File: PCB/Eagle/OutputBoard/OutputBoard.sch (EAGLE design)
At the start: 19 parts

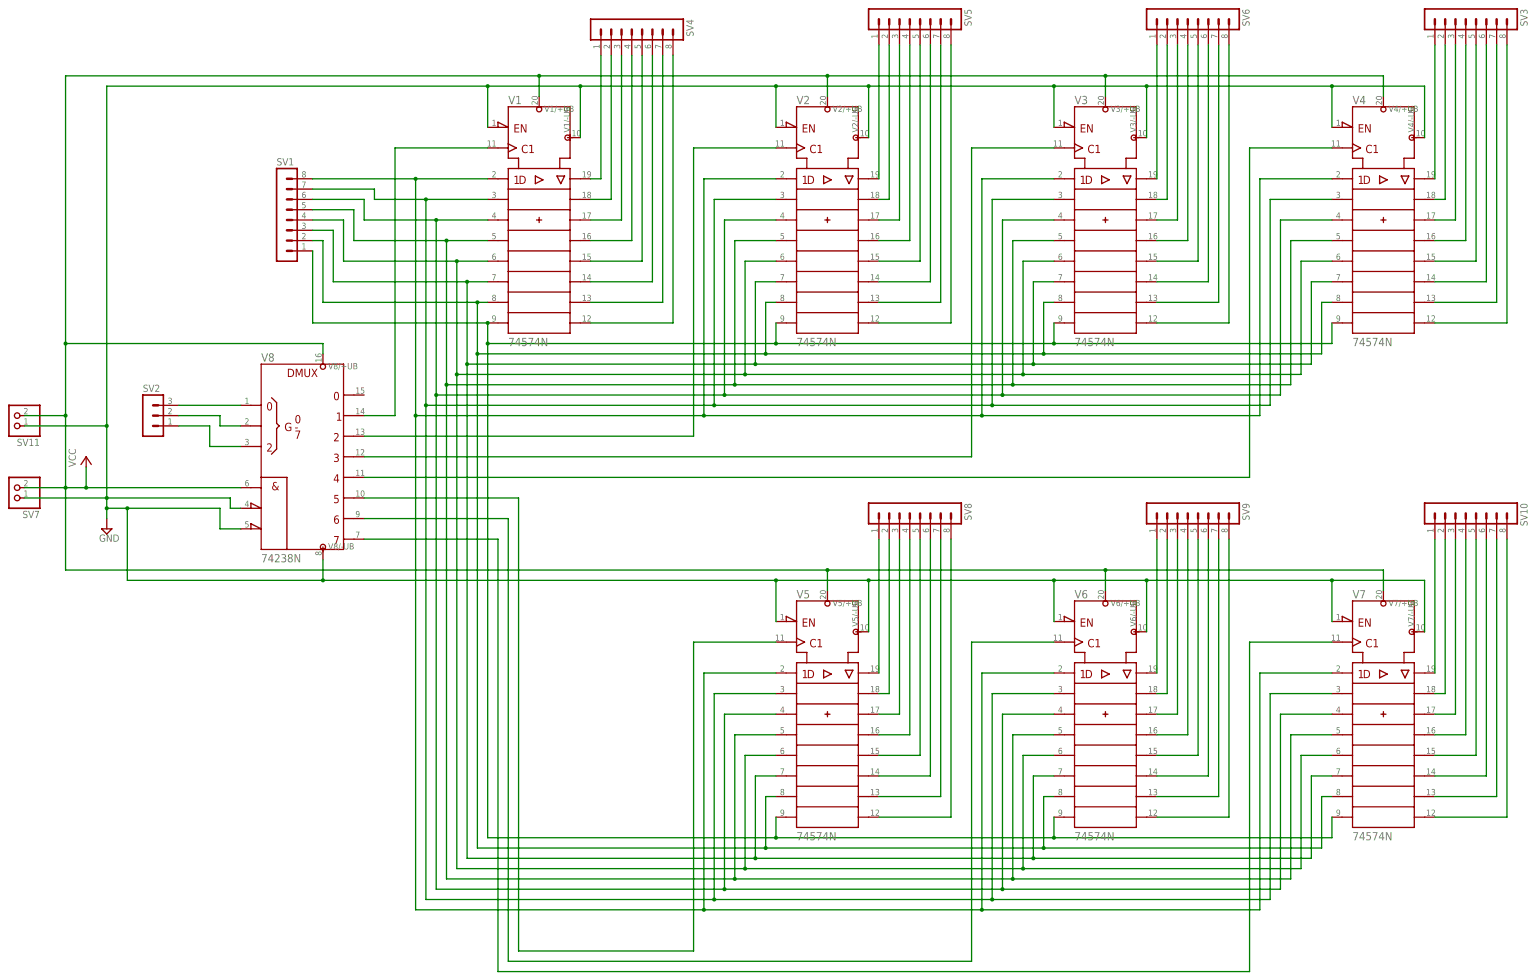
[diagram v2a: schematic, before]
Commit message: PCB Modified with proper flip flop 74 273 and ground fill
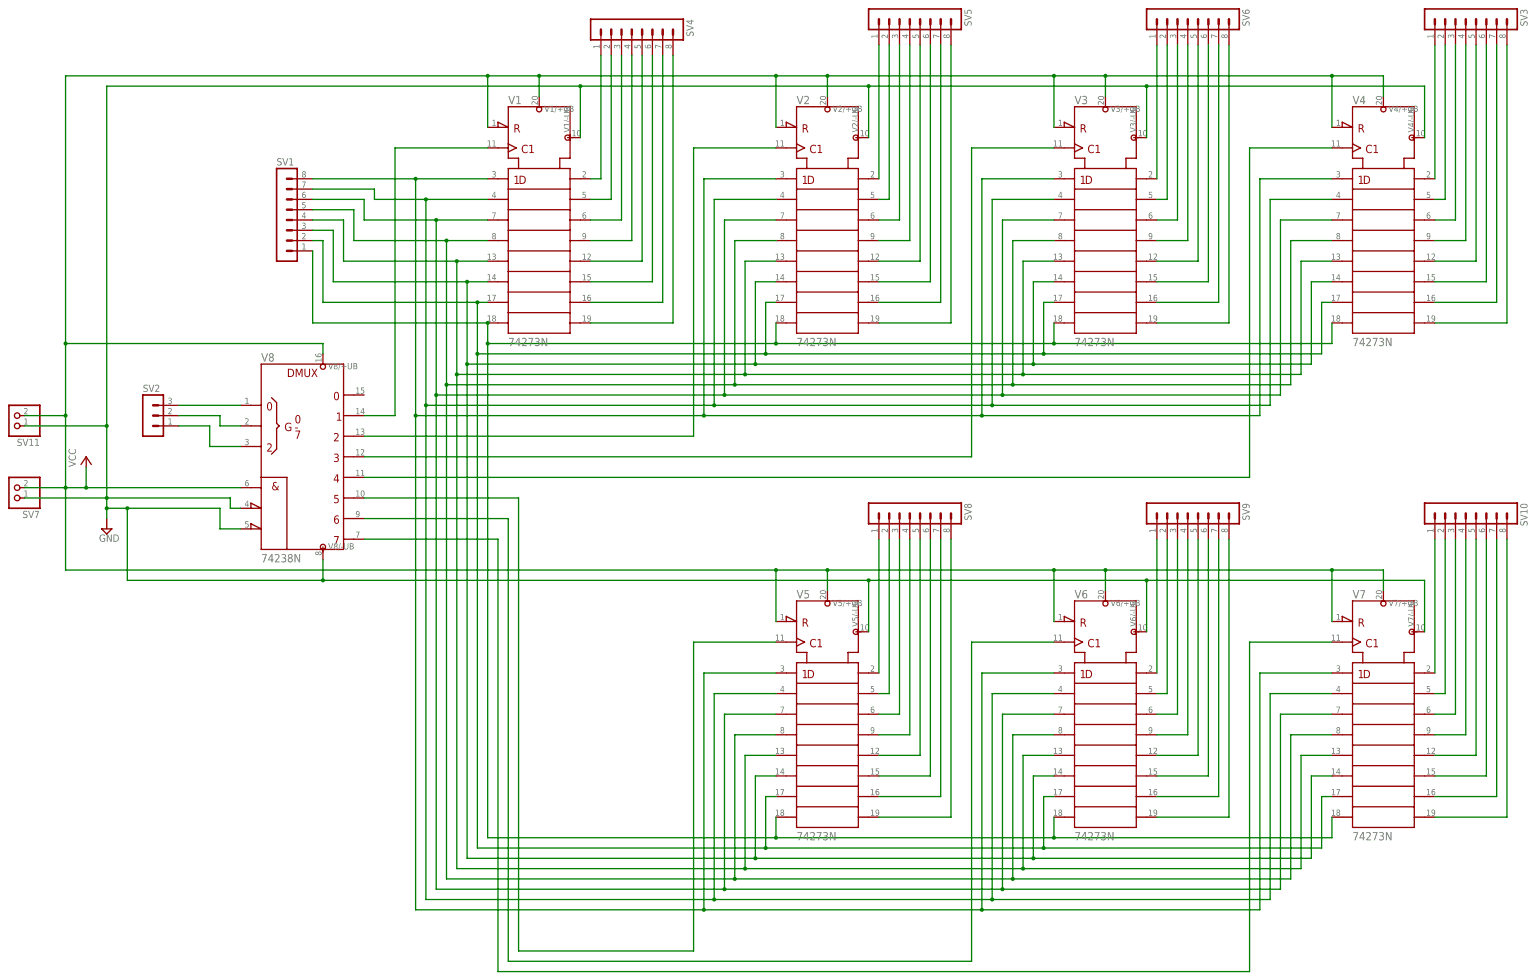
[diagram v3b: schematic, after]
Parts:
- V1, V2, V3, V4, V5, V6, V7: value 74574N -> 74273N; device 74ttl-din:74574N -> 74ttl-din:74273N
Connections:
- net GND: no longer V11.!OC, V21.!OC, V31.!OC, V41.!OC, V51.!OC, V61.!OC, V71.!OC
- net VCC: now also V11.!CLR, V21.!CLR, V31.!CLR, V41.!CLR, V51.!CLR, V61.!CLR, V71.!CLR
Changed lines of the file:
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@@
 </classes>
 <parts>
-<part name="V1" library="74ttl-din" deviceset="74*574" device="N"/>
-<part name="V2" library="74ttl-din" deviceset="74*574" device="N"/>
-<part name="V3" library="74ttl-din" deviceset="74*574" device="N"/>
+<part name="V1" library="74ttl-din" deviceset="74*273" device="N"/>
+<part name="V2" library="74ttl-din" deviceset="74*273" device="N"/>
+<part name="V3" library="74ttl-din" deviceset="74*273" device="N"/>
 <part name="SUPPLY1" library="supply2" deviceset="GND" device=""/>
 <part name="P+1" library="supply1" deviceset="VCC" device=""/>
@@
 <part name="SV6" library="con-lstb" deviceset="MA08-1" device=""/>
 <part name="SV7" library="pinhead" deviceset="PINHD-1X2" device=""/>
-<part name="V4" library="74ttl-din" deviceset="74*574" device="N"/>
+<part name="V4" library="74ttl-din" deviceset="74*273" device="N"/>
 <part name="SV3" library="con-lstb" deviceset="MA08-1" device=""/>
-<part name="V5" library="74ttl-din" deviceset="74*574" device="N"/>
-<part name="V6" library="74ttl-din" deviceset="74*574" device="N"/>
+<part name="V5" library="74ttl-din" deviceset="74*273" device="N"/>
+<part name="V6" library="74ttl-din" deviceset="74*273" device="N"/>
 <part name="SV8" library="con-lstb" deviceset="MA08-1" device=""/>
 <part name="SV9" library="con-lstb" deviceset="MA08-1" device=""/>
-<part name="V7" library="74ttl-din" deviceset="74*574" device="N"/>
+<part name="V7" library="74ttl-din" deviceset="74*273" device="N"/>
 <part name="SV10" library="con-lstb" deviceset="MA08-1" device=""/>
 <part name="V8" library="74ttl-din" deviceset="74*238" device="N"/>
@@
 <net name="GND" class="0">
 <segment>
-<pinref part="V1" gate="1" pin="!OC"/>
-<wire x1="35.56" y1="68.58" x2="35.56" y2="78.74" width="0.1524" layer="91"/>
-<wire x1="-58.42" y1="78.74" x2="35.56" y2="78.74" width="0.1524" layer="91"/>
-<junction x="35.56" y="78.74"/>
+<wire x1="-58.42" y1="78.74" x2="58.42" y2="78.74" width="0.1524" layer="91"/>
 <pinref part="SUPPLY1" gate="GND" pin="GND"/>
 <wire x1="-58.42" y1="-27.94" x2="-58.42" y2="-25.4" width="0.1524" layer="91"/>
@@
 <pinref part="SV7" gate="G$1" pin="1"/>
 <wire x1="-78.74" y1="-22.86" x2="-58.42" y2="-22.86" width="0.1524" layer="91"/>
-<pinref part="V5" gate="1" pin="!OC"/>
-<wire x1="106.68" y1="-43.18" x2="106.68" y2="-53.34" width="0.1524" layer="91"/>
-<wire x1="106.68" y1="-43.18" x2="129.54" y2="-43.18" width="0.1524" layer="91"/>
-<pinref part="V6" gate="1" pin="!OC"/>
-<wire x1="129.54" y1="-43.18" x2="175.26" y2="-43.18" width="0.1524" layer="91"/>
-<wire x1="175.26" y1="-43.18" x2="175.26" y2="-53.34" width="0.1524" layer="91"/>
-<junction x="106.68" y="-43.18"/>
-<wire x1="175.26" y1="-43.18" x2="198.12" y2="-43.18" width="0.1524" layer="91"/>
-<pinref part="V7" gate="1" pin="!OC"/>
-<wire x1="198.12" y1="-43.18" x2="243.84" y2="-43.18" width="0.1524" layer="91"/>
-<wire x1="243.84" y1="-43.18" x2="243.84" y2="-53.34" width="0.1524" layer="91"/>
-<junction x="175.26" y="-43.18"/>
-<wire x1="106.68" y1="-43.18" x2="-5.08" y2="-43.18" width="0.1524" layer="91"/>
+<wire x1="129.54" y1="-43.18" x2="198.12" y2="-43.18" width="0.1524" layer="91"/>
+<wire x1="198.12" y1="-43.18" x2="266.7" y2="-43.18" width="0.1524" layer="91"/>
+<wire x1="129.54" y1="-43.18" x2="-5.08" y2="-43.18" width="0.1524" layer="91"/>
 <wire x1="-5.08" y1="-43.18" x2="-53.34" y2="-43.18" width="0.1524" layer="91"/>
 <wire x1="-53.34" y1="-43.18" x2="-53.34" y2="-25.4" width="0.1524" layer="91"/>
-<pinref part="V4" gate="1" pin="!OC"/>
-<wire x1="243.84" y1="78.74" x2="243.84" y2="68.58" width="0.1524" layer="91"/>
-<pinref part="V3" gate="1" pin="!OC"/>
-<pinref part="V2" gate="1" pin="!OC"/>
-<wire x1="35.56" y1="78.74" x2="58.42" y2="78.74" width="0.1524" layer="91"/>
-<wire x1="58.42" y1="78.74" x2="106.68" y2="78.74" width="0.1524" layer="91"/>
-<wire x1="106.68" y1="78.74" x2="106.68" y2="68.58" width="0.1524" layer="91"/>
-<junction x="106.68" y="78.74"/>
-<wire x1="106.68" y1="78.74" x2="129.54" y2="78.74" width="0.1524" layer="91"/>
-<wire x1="129.54" y1="78.74" x2="175.26" y2="78.74" width="0.1524" layer="91"/>
-<wire x1="175.26" y1="78.74" x2="175.26" y2="68.58" width="0.1524" layer="91"/>
-<wire x1="175.26" y1="78.74" x2="198.12" y2="78.74" width="0.1524" layer="91"/>
-<junction x="175.26" y="78.74"/>
-<wire x1="198.12" y1="78.74" x2="243.84" y2="78.74" width="0.1524" layer="91"/>
+<wire x1="58.42" y1="78.74" x2="129.54" y2="78.74" width="0.1524" layer="91"/>
+<wire x1="129.54" y1="78.74" x2="198.12" y2="78.74" width="0.1524" layer="91"/>
+<wire x1="198.12" y1="78.74" x2="266.7" y2="78.74" width="0.1524" layer="91"/>
 <wire x1="-58.42" y1="-22.86" x2="-27.94" y2="-22.86" width="0.1524" layer="91"/>
 <wire x1="-27.94" y1="-22.86" x2="-27.94" y2="-25.4" width="0.1524" layer="91"/>
@@
 <wire x1="198.12" y1="66.04" x2="198.12" y2="78.74" width="0.1524" layer="91"/>
 <junction x="198.12" y="78.74"/>
-<wire x1="243.84" y1="78.74" x2="266.7" y2="78.74" width="0.1524" layer="91"/>
-<junction x="243.84" y="78.74"/>
 <pinref part="V4" gate="/-UB" pin="-UB"/>
 <wire x1="266.7" y1="78.74" x2="266.7" y2="66.04" width="0.1524" layer="91"/>
@@
 <wire x1="198.12" y1="-55.88" x2="198.12" y2="-43.18" width="0.1524" layer="91"/>
 <junction x="198.12" y="-43.18"/>
-<wire x1="243.84" y1="-43.18" x2="266.7" y2="-43.18" width="0.1524" layer="91"/>
-<junction x="243.84" y="-43.18"/>
 <pinref part="V7" gate="/-UB" pin="-UB"/>
 <wire x1="266.7" y1="-43.18" x2="266.7" y2="-55.88" width="0.1524" layer="91"/>
@@
 <wire x1="-68.58" y1="-2.54" x2="-68.58" y2="15.24" width="0.1524" layer="91"/>
 <wire x1="-68.58" y1="15.24" x2="-68.58" y2="81.28" width="0.1524" layer="91"/>
-<wire x1="-68.58" y1="81.28" x2="48.26" y2="81.28" width="0.1524" layer="91"/>
 <pinref part="V1" gate="/+UB" pin="+UB"/>
+<wire x1="-68.58" y1="81.28" x2="35.56" y2="81.28" width="0.1524" layer="91"/>
+<wire x1="35.56" y1="81.28" x2="48.26" y2="81.28" width="0.1524" layer="91"/>
 <wire x1="48.26" y1="81.28" x2="48.26" y2="76.2" width="0.1524" layer="91"/>
 <pinref part="V8" gate="1" pin="G1"/>
@@
 <pinref part="V2" gate="/+UB" pin="+UB"/>
 <wire x1="119.38" y1="76.2" x2="119.38" y2="81.28" width="0.1524" layer="91"/>
-<wire x1="119.38" y1="81.28" x2="48.26" y2="81.28" width="0.1524" layer="91"/>
+<wire x1="119.38" y1="81.28" x2="106.68" y2="81.28" width="0.1524" layer="91"/>
 <junction x="48.26" y="81.28"/>
 <pinref part="V3" gate="/+UB" pin="+UB"/>
+<wire x1="106.68" y1="81.28" x2="48.26" y2="81.28" width="0.1524" layer="91"/>
 <wire x1="187.96" y1="76.2" x2="187.96" y2="81.28" width="0.1524" layer="91"/>
-<wire x1="187.96" y1="81.28" x2="119.38" y2="81.28" width="0.1524" layer="91"/>
+<wire x1="187.96" y1="81.28" x2="175.26" y2="81.28" width="0.1524" layer="91"/>
 <junction x="119.38" y="81.28"/>
 <pinref part="V4" gate="/+UB" pin="+UB"/>
+<wire x1="175.26" y1="81.28" x2="119.38" y2="81.28" width="0.1524" layer="91"/>
 <wire x1="256.54" y1="76.2" x2="256.54" y2="81.28" width="0.1524" layer="91"/>
-<wire x1="256.54" y1="81.28" x2="187.96" y2="81.28" width="0.1524" layer="91"/>
+<wire x1="256.54" y1="81.28" x2="243.84" y2="81.28" width="0.1524" layer="91"/>
 <junction x="187.96" y="81.28"/>
+<wire x1="243.84" y1="81.28" x2="187.96" y2="81.28" width="0.1524" layer="91"/>
 <wire x1="-68.58" y1="-20.32" x2="-68.58" y2="-40.64" width="0.1524" layer="91"/>
-<wire x1="-68.58" y1="-40.64" x2="119.38" y2="-40.64" width="0.1524" layer="91"/>
+<wire x1="-68.58" y1="-40.64" x2="106.68" y2="-40.64" width="0.1524" layer="91"/>
 <pinref part="V5" gate="/+UB" pin="+UB"/>
+<wire x1="106.68" y1="-40.64" x2="119.38" y2="-40.64" width="0.1524" layer="91"/>
 <wire x1="119.38" y1="-40.64" x2="119.38" y2="-45.72" width="0.1524" layer="91"/>
-<wire x1="119.38" y1="-40.64" x2="187.96" y2="-40.64" width="0.1524" layer="91"/>
+<wire x1="119.38" y1="-40.64" x2="175.26" y2="-40.64" width="0.1524" layer="91"/>
 <junction x="119.38" y="-40.64"/>
 <pinref part="V6" gate="/+UB" pin="+UB"/>
+<wire x1="175.26" y1="-40.64" x2="187.96" y2="-40.64" width="0.1524" layer="91"/>
 <wire x1="187.96" y1="-40.64" x2="187.96" y2="-45.72" width="0.1524" layer="91"/>
-<wire x1="187.96" y1="-40.64" x2="256.54" y2="-40.64" width="0.1524" layer="91"/>
+<wire x1="187.96" y1="-40.64" x2="243.84" y2="-40.64" width="0.1524" layer="91"/>
 <junction x="187.96" y="-40.64"/>
 <pinref part="V7" gate="/+UB" pin="+UB"/>
+<wire x1="243.84" y1="-40.64" x2="256.54" y2="-40.64" width="0.1524" layer="91"/>
 <wire x1="256.54" y1="-40.64" x2="256.54" y2="-45.72" width="0.1524" layer="91"/>
 <pinref part="V8" gate="/+UB" pin="+UB"/>
@@
 <wire x1="-78.74" y1="-2.54" x2="-68.58" y2="-2.54" width="0.1524" layer="91"/>
 <junction x="-68.58" y="-2.54"/>
+<pinref part="V2" gate="1" pin="!CLR"/>
+<wire x1="106.68" y1="68.58" x2="106.68" y2="81.28" width="0.1524" layer="91"/>
+<junction x="106.68" y="81.28"/>
+<pinref part="V1" gate="1" pin="!CLR"/>
+<wire x1="35.56" y1="68.58" x2="35.56" y2="81.28" width="0.1524" layer="91"/>
+<junction x="35.56" y="81.28"/>
+<pinref part="V3" gate="1" pin="!CLR"/>
+<wire x1="175.26" y1="68.58" x2="175.26" y2="81.28" width="0.1524" layer="91"/>
+<junction x="175.26" y="81.28"/>
+<pinref part="V4" gate="1" pin="!CLR"/>
+<wire x1="243.84" y1="68.58" x2="243.84" y2="81.28" width="0.1524" layer="91"/>
+<junction x="243.84" y="81.28"/>
+<pinref part="V5" gate="1" pin="!CLR"/>
+<wire x1="106.68" y1="-53.34" x2="106.68" y2="-40.64" width="0.1524" layer="91"/>
+<junction x="106.68" y="-40.64"/>
+<pinref part="V6" gate="1" pin="!CLR"/>
+<wire x1="175.26" y1="-53.34" x2="175.26" y2="-40.64" width="0.1524" layer="91"/>
+<junction x="175.26" y="-40.64"/>
+<pinref part="V7" gate="1" pin="!CLR"/>
+<wire x1="243.84" y1="-53.34" x2="243.84" y2="-40.64" width="0.1524" layer="91"/>
+<junction x="243.84" y="-40.64"/>
 </segment>
 </net>
@@
 </sheet>
 </sheets>
+<errors>
+</errors>
 </schematic>
 </drawing>
